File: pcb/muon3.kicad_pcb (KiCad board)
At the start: 4 copper layers, 120 x 90 mm, 0 parts

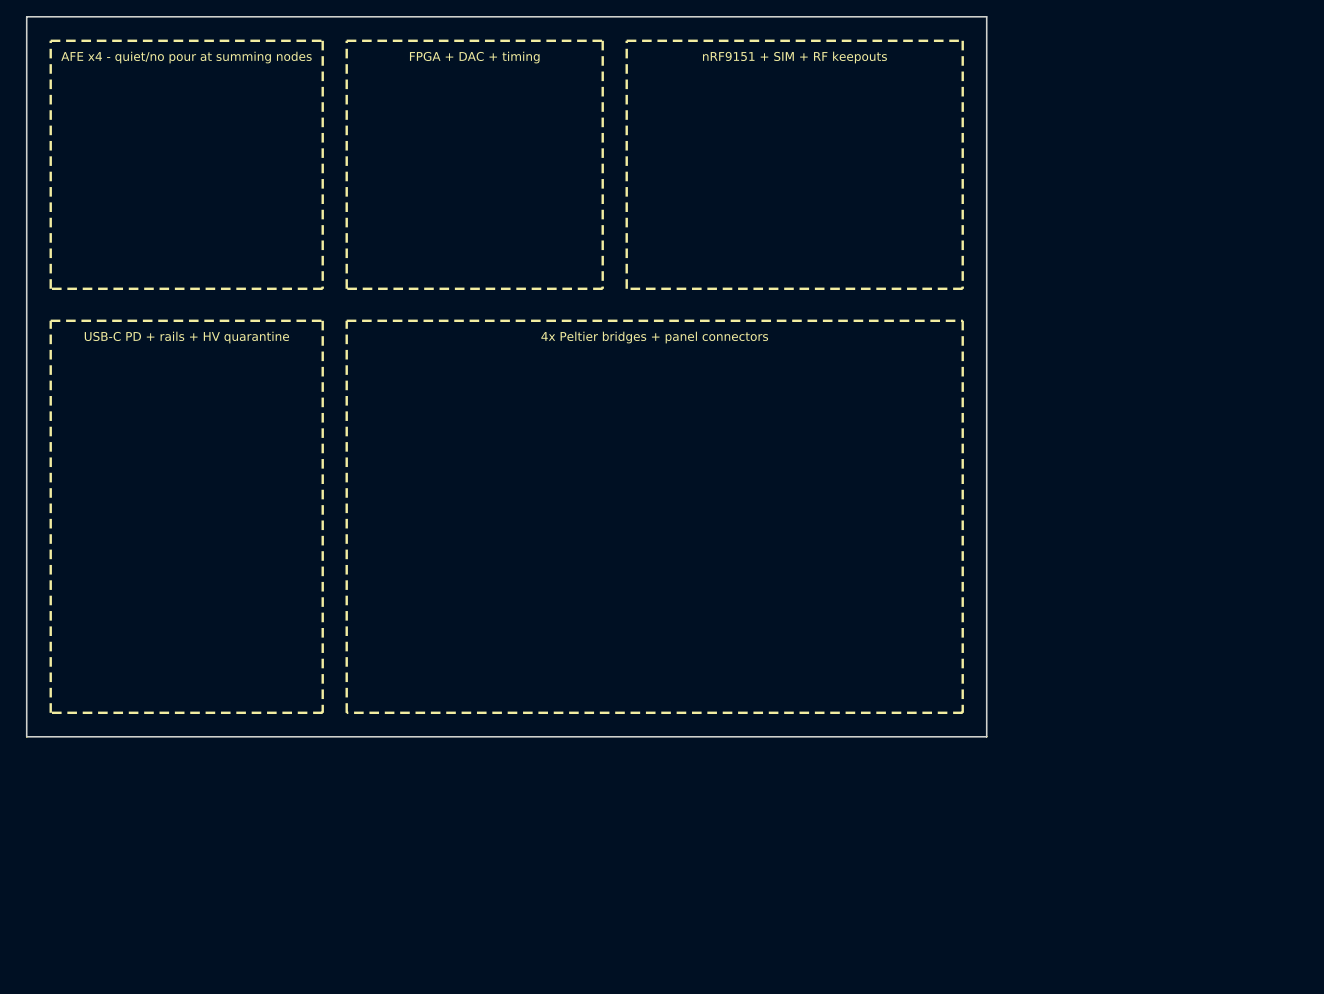
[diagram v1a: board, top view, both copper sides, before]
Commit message: Add tscircuit placement/autorouter bridge into KiCad
Wire Muon3 tscircuit placement and the capacity autorouter into the KiCad
workflow: export circuit-json to a reference KiCad project, stamp zone
fences/keepouts into muon3.kicad_pcb, run a netted autoroute demo, and
document the full bridge (coords, scripts, limits for RF/AFE/HV).
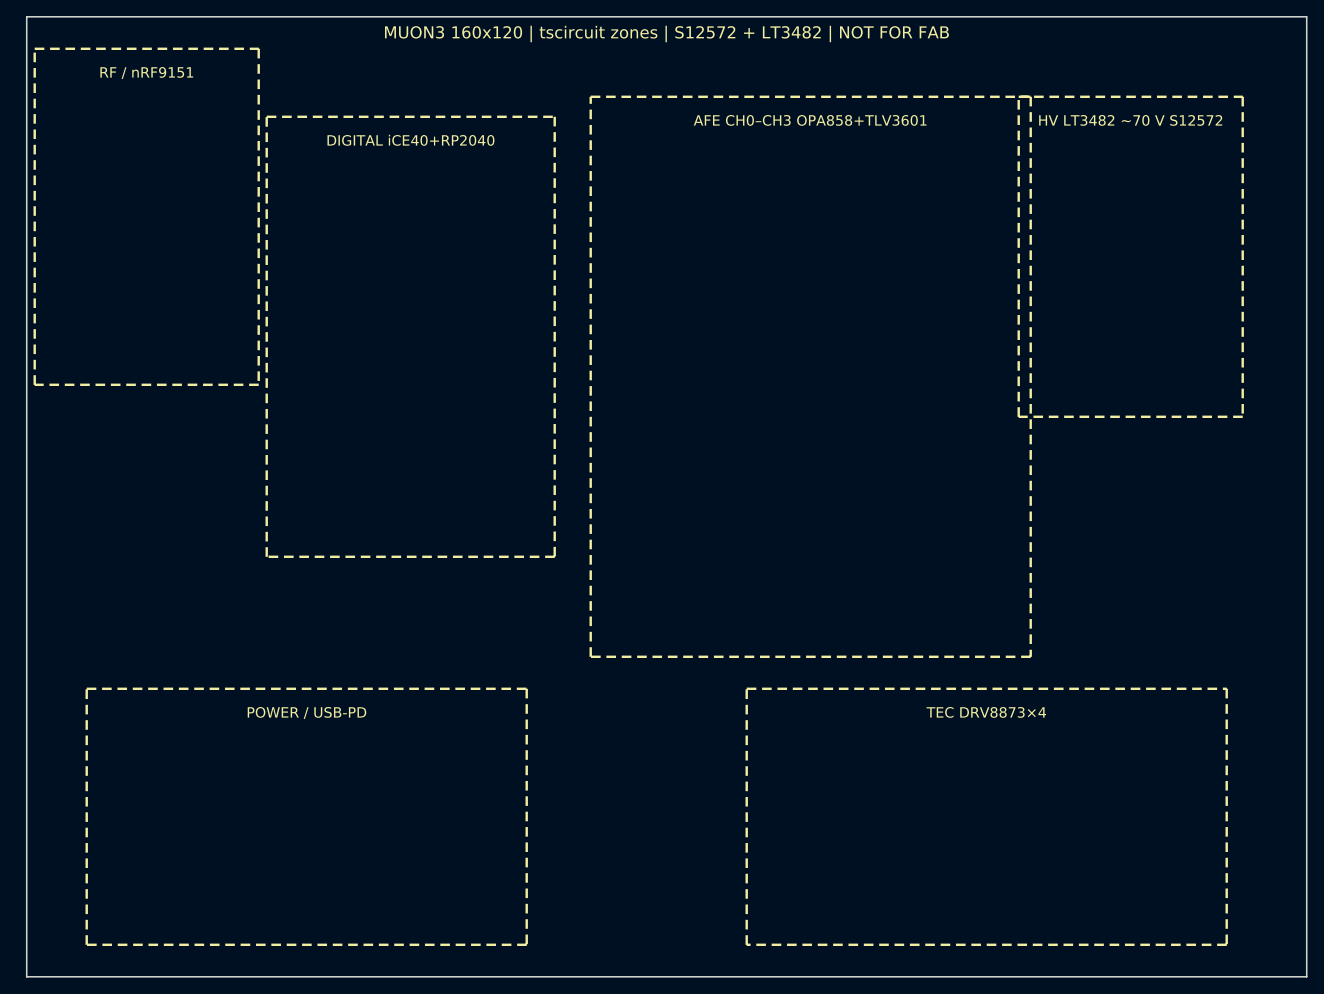
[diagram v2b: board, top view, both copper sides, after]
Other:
- board size 120 x 90 mm -> 160 x 120 mm
- board text added: "#TSCIRCUIT_PLACEMENT_BEGIN"
- board text added: "#TSCIRCUIT_PLACEMENT_END"
- board text added: "AFE CH0–CH3 OPA858+TLV3601"
- board text added: "AFE shield fence / can over TIA banks"
- board text added: "ANT KEEPOUT 15mm"
- board text added: "DIGITAL iCE40+RP2040"
- board text added: "HV LT3482 ~70 V S12572"
- board text added: "HV SW NODE KEEPOUT"
- board text added: "HV keepout; no pour under boost SW node"
- board text added: "MUON3 160x120 | tscircuit zones | S12572 + LT3482 | NOT FOR FAB"
- board text added: "Muon3 tscircuit zones 160x120mm — regen: bun run sync:zones"
- board text added: "POWER / USB-PD"
- board text added: "RF / nRF9151"
- board text added: "RF shield can optional; antenna keepout 15 mm"
- board text added: "Switching zone; short loops; far from AFE"
- board text added: "TEC DRV8873×4"
- board text added: "TIA CH0 NO POUR"
- board text added: "TIA CH1 NO POUR"
- board text added: "TIA CH2 NO POUR"
- board text added: "TIA CH3 NO POUR"
- board text removed: "4x Peltier bridges + panel connectors"
- board text removed: "AFE x4 - quiet/no pour at summing nodes"
- board text removed: "FPGA + DAC + timing"
- board text removed: "MUON3 P0 ARCHITECTURE - NOT FOR FABRICATION"
- board text removed: "USB-C PD + rails + HV quarantine"
- board text removed: "nRF9151 + SIM + RF keepouts"
